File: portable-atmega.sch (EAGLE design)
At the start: 35 parts

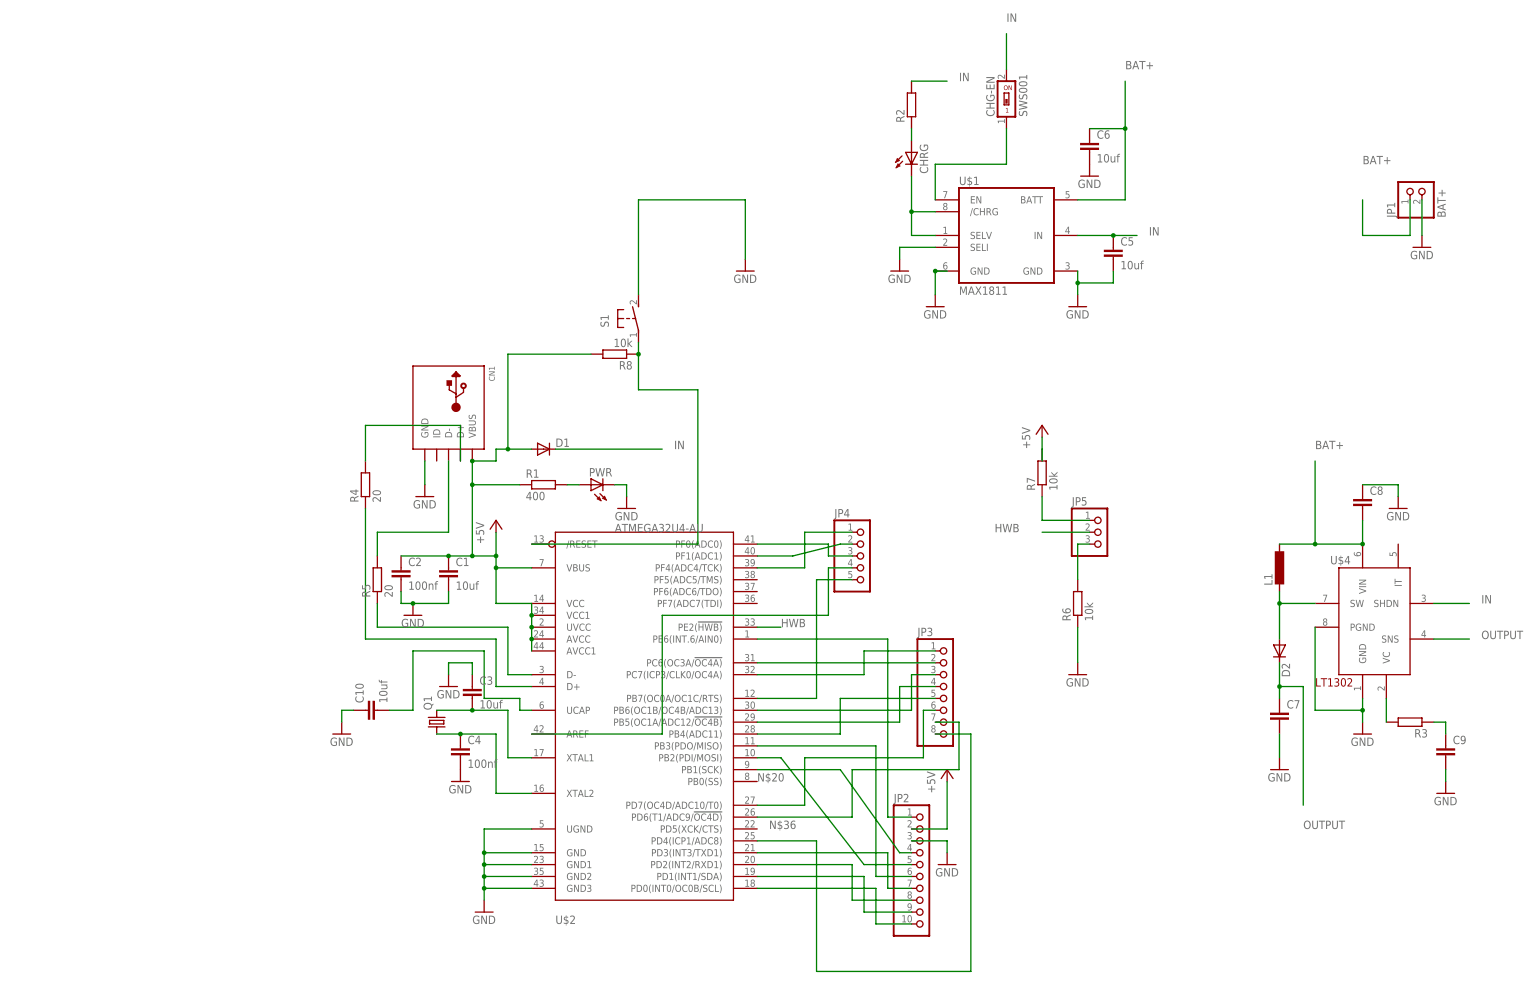
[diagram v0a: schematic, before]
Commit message: Updated Schematic and BRD
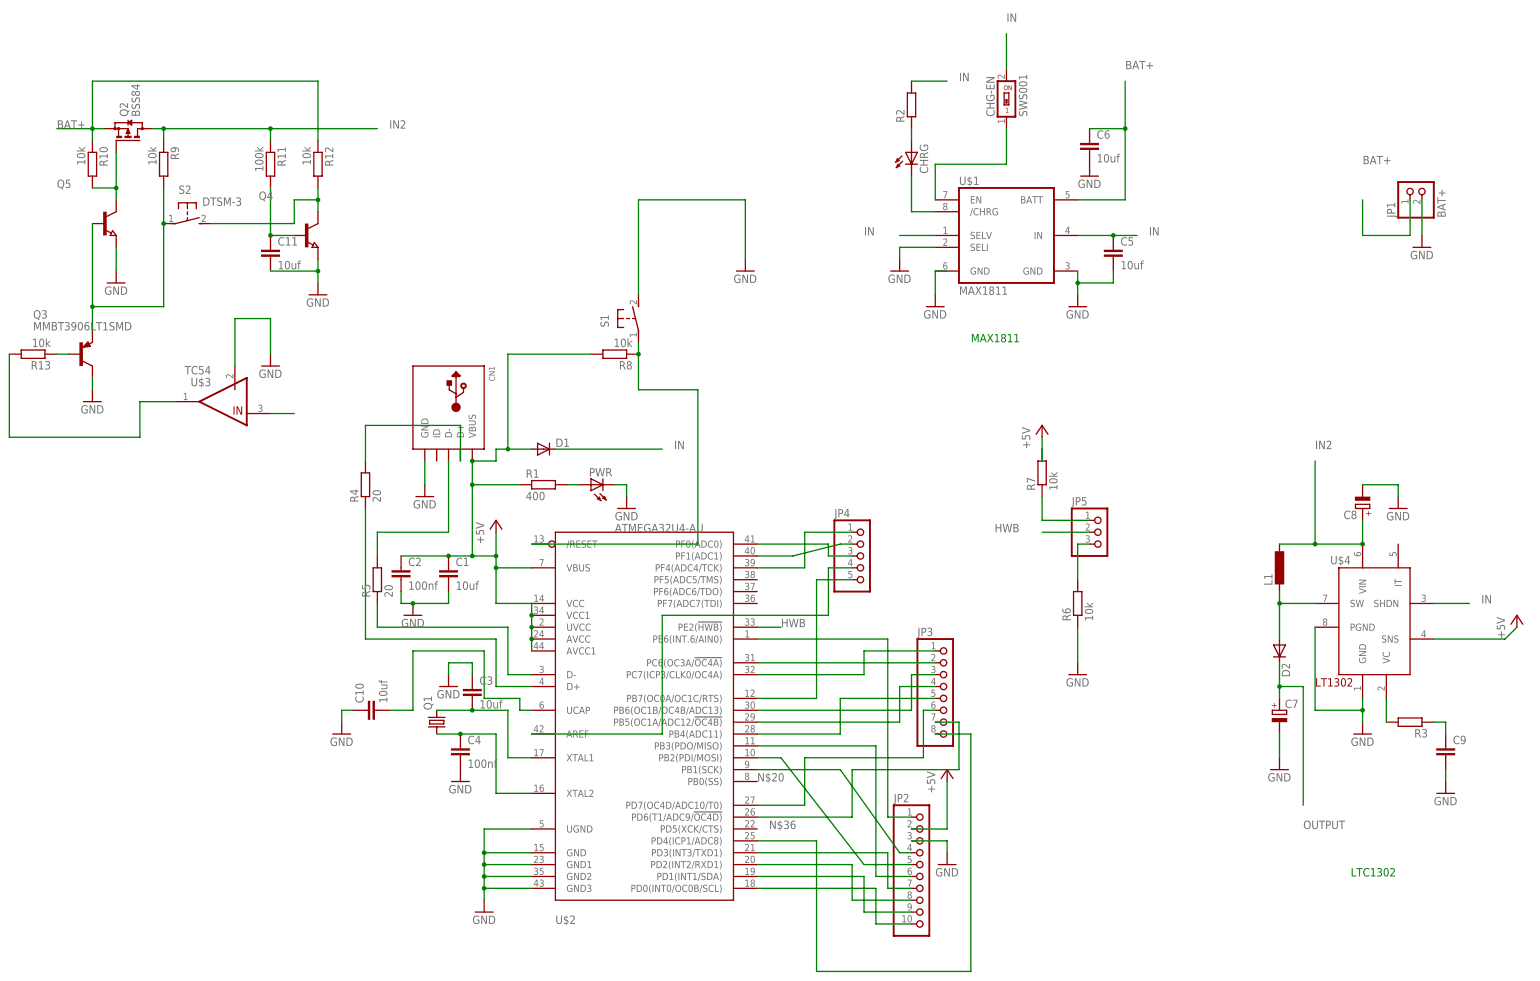
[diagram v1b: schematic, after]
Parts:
- added C11: 10uf, resistor:C-EUC1206
- added Q2: BSS84, transistor-small-signal:BSS84
- added Q3: MMBT3906LT1SMD, transistor-pnp:MMBT3906LT1SMD
- added Q4, Q5: (no value), semicon-smd-ipc:NPN-TRANSISTOR_SOT23
- added R10, R12: 10k, resistor:R-EU_R1206
- added R11: 100k, solar3-1:R-EU_R0805
- added R13, R9: 10k, solar3-1:R-EU_R0805
- added S2: DTSM-3, switch-tact:DTSM-3
- added U$3: TC54, microchip:TC54
- C7: device resistor:C-EUC3225 -> resistor:CPOL-EUD
- C8: device resistor:C-EUC1206 -> resistor:CPOL-EUD
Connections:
- new net IN2: C8.+, L1.2, Q2.D, R11.1, R9.1, U$4.VIN
- new net N$39: Q2.G, Q5.C, R10.2
- new net N$40: Q3.E, Q5.B, R9.2, S2.1
- new net N$42: C11.1, Q4.B, R11.2
- new net N$43: Q4.C, R12.2, S2.2
- new net N$46: R13.2, U$3.VOUT
- new net N$47: Q3.B, R13.1
- net +5V: now also U$4.SNS
- net BAT+: now also Q2.S, R10.1, R12.1, U$3.VIN; no longer C8.2, L1.2, U$4.VIN
- net GND: now also C11.2, C7.-, C8.-, Q3.C, Q4.E, Q5.E, U$3.VSS; no longer C7.2, C8.1
- net IN: now also U$1.SELV
- net N$4: no longer U$1.SELV
- net OUTPUT: now also C7.+; no longer C7.1, U$4.SNS
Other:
- note added: "LTC1302"
- note added: "MAX1811"
